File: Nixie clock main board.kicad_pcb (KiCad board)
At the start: 2 copper layers, 135 x 60 mm, 34 parts, among them J1 Vin, J2 TIMEZONE-, J3 TIMEZONE+, J4 PROG, J5 12V_AC_rectified, J6 6P6C, J7 GPS, Q1 BSS84, U1 LM2576T-5, U2 MCP1825S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

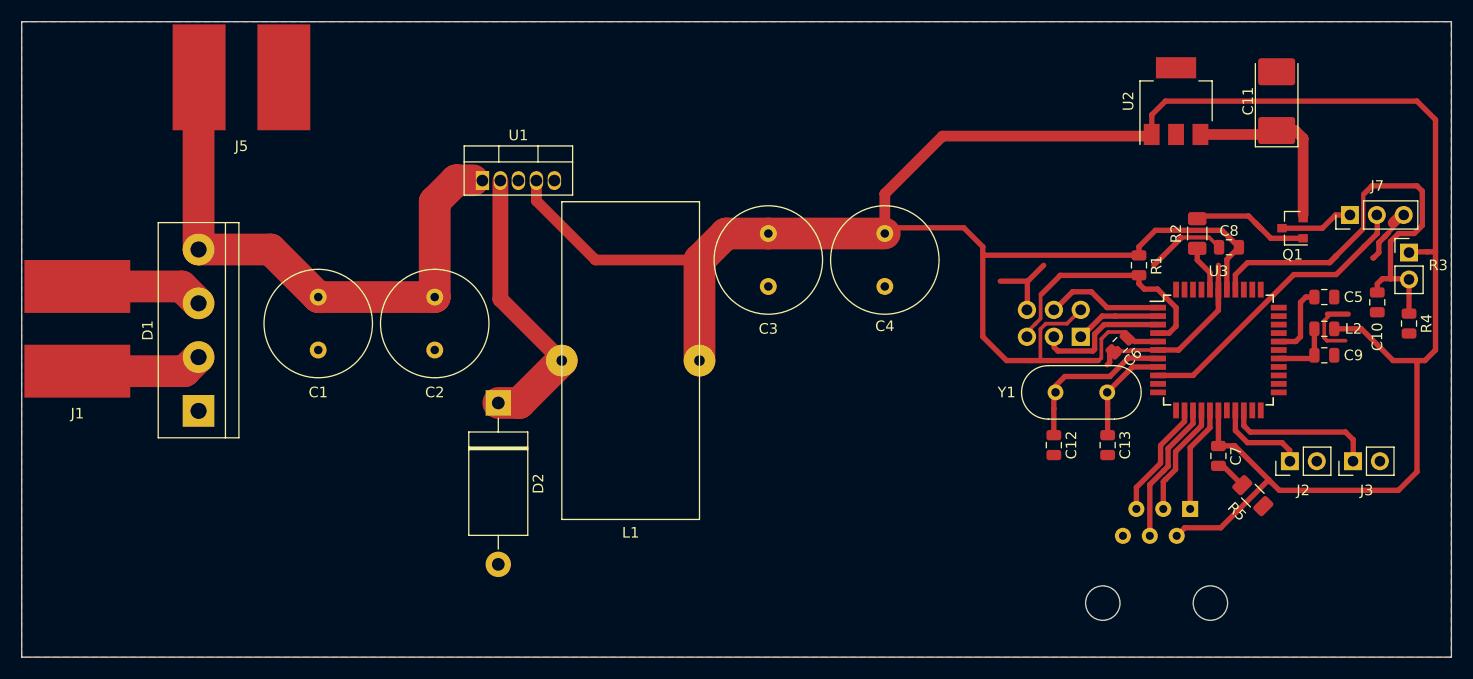
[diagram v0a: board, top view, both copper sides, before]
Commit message: Added mounting holes
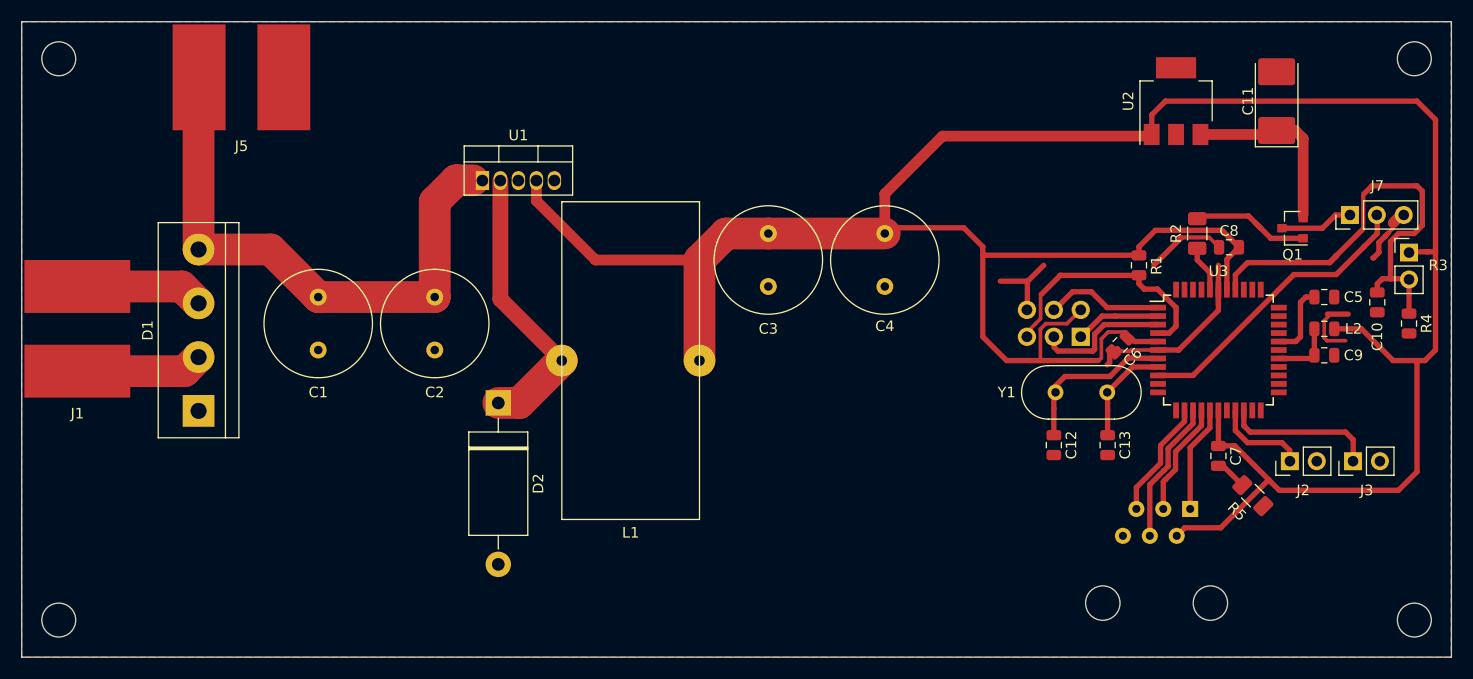
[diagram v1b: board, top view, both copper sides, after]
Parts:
- added 3mm hole: MountingHole_3.2mm_M3_DIN965, MountingHole:MountingHole_3.2mm_M3_DIN965, F.Cu at (153.5, 74.5)
- added 3mm hole: MountingHole_3.2mm_M3_DIN965, MountingHole:MountingHole_3.2mm_M3_DIN965, F.Cu at (153.5, 21.5)
- added 3mm hole: MountingHole_3.2mm_M3_DIN965, MountingHole:MountingHole_3.2mm_M3_DIN965, F.Cu at (25.5, 74.5)
- added 3mm hole: MountingHole_3.2mm_M3_DIN965, MountingHole:MountingHole_3.2mm_M3_DIN965, F.Cu at (25.5, 21.5)
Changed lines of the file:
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@@
     (tracks 245)
     (zones 0)
-    (modules 34)
+    (modules 38)
     (nets 48)
   )
@@
     (diff_pair_gap 0.25)
   )
+  (module MountingHole:MountingHole_3.2mm_M3_DIN965 (layer Top)
+    (at 153.5 74.5)
+    (descr "Mounting Hole 3.2mm, no annular, M3, DIN965")
+    (tags "mounting hole 3.2mm no annular m3 din965")
+    (attr virtual)
+    (fp_text reference "3mm hole" (at 0 4.5) (layer F.SilkS) hide
+      (effects (font (size 1 1) (thickness 0.15)))
+    )
+    (fp_text value MountingHole_3.2mm_M3_DIN965 (at 0 3.8) (layer F.Fab)
+      (effects (font (size 1 1) (thickness 0.15)))
+    )
+    (fp_circle (center 0 0) (end 3.05 0) (layer F.CrtYd) (width 0.05))
+    (fp_circle (center 0 0) (end 2.8 0) (layer Cmts.User) (width 0.15))
+    (fp_text user %R (at 0.3 0) (layer F.Fab)
+      (effects (font (size 1 1) (thickness 0.15)))
+    )
+    (pad 1 np_thru_hole circle (at 0 0) (size 3.2 3.2) (drill 3.2) (layers *.Cu *.Mask))
+  )
+  (module MountingHole:MountingHole_3.2mm_M3_DIN965 (layer Top)
+    (at 153.5 21.5)
+    (descr "Mounting Hole 3.2mm, no annular, M3, DIN965")
+    (tags "mounting hole 3.2mm no annular m3 din965")
+    (attr virtual)
+    (fp_text reference "3mm hole" (at 0 -4.5) (layer F.SilkS) hide
+      (effects (font (size 1 1) (thickness 0.15)))
+    )
+    (fp_text value MountingHole_3.2mm_M3_DIN965 (at 0 3.8) (layer F.Fab)
+      (effects (font (size 1 1) (thickness 0.15)))
+    )
+    (fp_circle (center 0 0) (end 3.05 0) (layer F.CrtYd) (width 0.05))
+    (fp_circle (center 0 0) (end 2.8 0) (layer Cmts.User) (width 0.15))
+    (fp_text user %R (at 0.3 0) (layer F.Fab)
+      (effects (font (size 1 1) (thickness 0.15)))
+    )
+    (pad 1 np_thru_hole circle (at 0 0) (size 3.2 3.2) (drill 3.2) (layers *.Cu *.Mask))
+  )
+  (module MountingHole:MountingHole_3.2mm_M3_DIN965 (layer Top)
+    (at 25.5 74.5)
+    (descr "Mounting Hole 3.2mm, no annular, M3, DIN965")
+    (tags "mounting hole 3.2mm no annular m3 din965")
+    (attr virtual)
+    (fp_text reference "3mm hole" (at 0 4.5) (layer F.SilkS) hide
+      (effects (font (size 1 1) (thickness 0.15)))
+    )
+    (fp_text value MountingHole_3.2mm_M3_DIN965 (at 0 3.8) (layer F.Fab)
+      (effects (font (size 1 1) (thickness 0.15)))
+    )
+    (fp_circle (center 0 0) (end 3.05 0) (layer F.CrtYd) (width 0.05))
+    (fp_circle (center 0 0) (end 2.8 0) (layer Cmts.User) (width 0.15))
+    (fp_text user %R (at 0.3 0) (layer F.Fab)
+      (effects (font (size 1 1) (thickness 0.15)))
+    )
+    (pad 1 np_thru_hole circle (at 0 0) (size 3.2 3.2) (drill 3.2) (layers *.Cu *.Mask))
+  )
+  (module MountingHole:MountingHole_3.2mm_M3_DIN965 (layer Top)
+    (at 25.5 21.5)
+    (descr "Mounting Hole 3.2mm, no annular, M3, DIN965")
+    (tags "mounting hole 3.2mm no annular m3 din965")
+    (attr virtual)
+    (fp_text reference "3mm hole" (at 0 -4.5) (layer F.SilkS) hide
+      (effects (font (size 1 1) (thickness 0.15)))
+    )
+    (fp_text value MountingHole_3.2mm_M3_DIN965 (at 0 3.8) (layer F.Fab)
+      (effects (font (size 1 1) (thickness 0.15)))
+    )
+    (fp_circle (center 0 0) (end 3.05 0) (layer F.CrtYd) (width 0.05))
+    (fp_circle (center 0 0) (end 2.8 0) (layer Cmts.User) (width 0.15))
+    (fp_text user %R (at 0.3 0) (layer F.Fab)
+      (effects (font (size 1 1) (thickness 0.15)))
+    )
+    (pad 1 np_thru_hole circle (at 0 0) (size 3.2 3.2) (drill 3.2) (layers *.Cu *.Mask))
+  )
   (module Connector_RJ:RJ12_Amphenol_54601 (layer Bottom)
